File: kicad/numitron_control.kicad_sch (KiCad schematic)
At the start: 12 parts, among them U1 TLC5916IN, U2 IV-12, U3 TLC5916IN, U4 IV-12, U5 TLC5916IN, U6 IV-12, U7 TLC5916IN, U8 IV-12

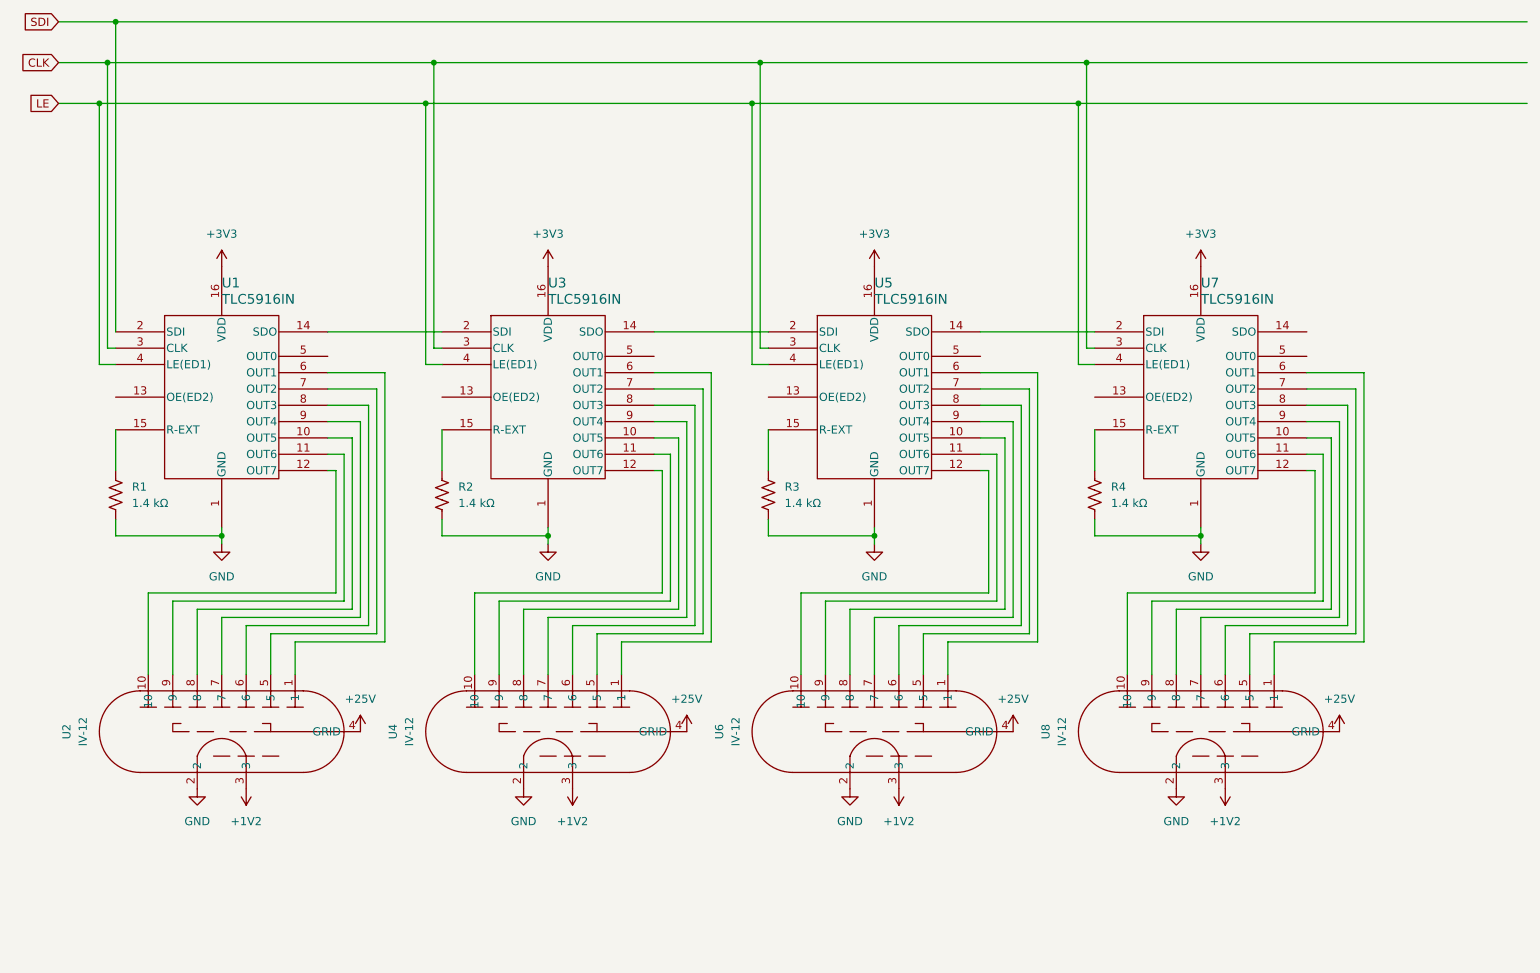
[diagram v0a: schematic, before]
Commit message: added voltage regulators, changed bit register
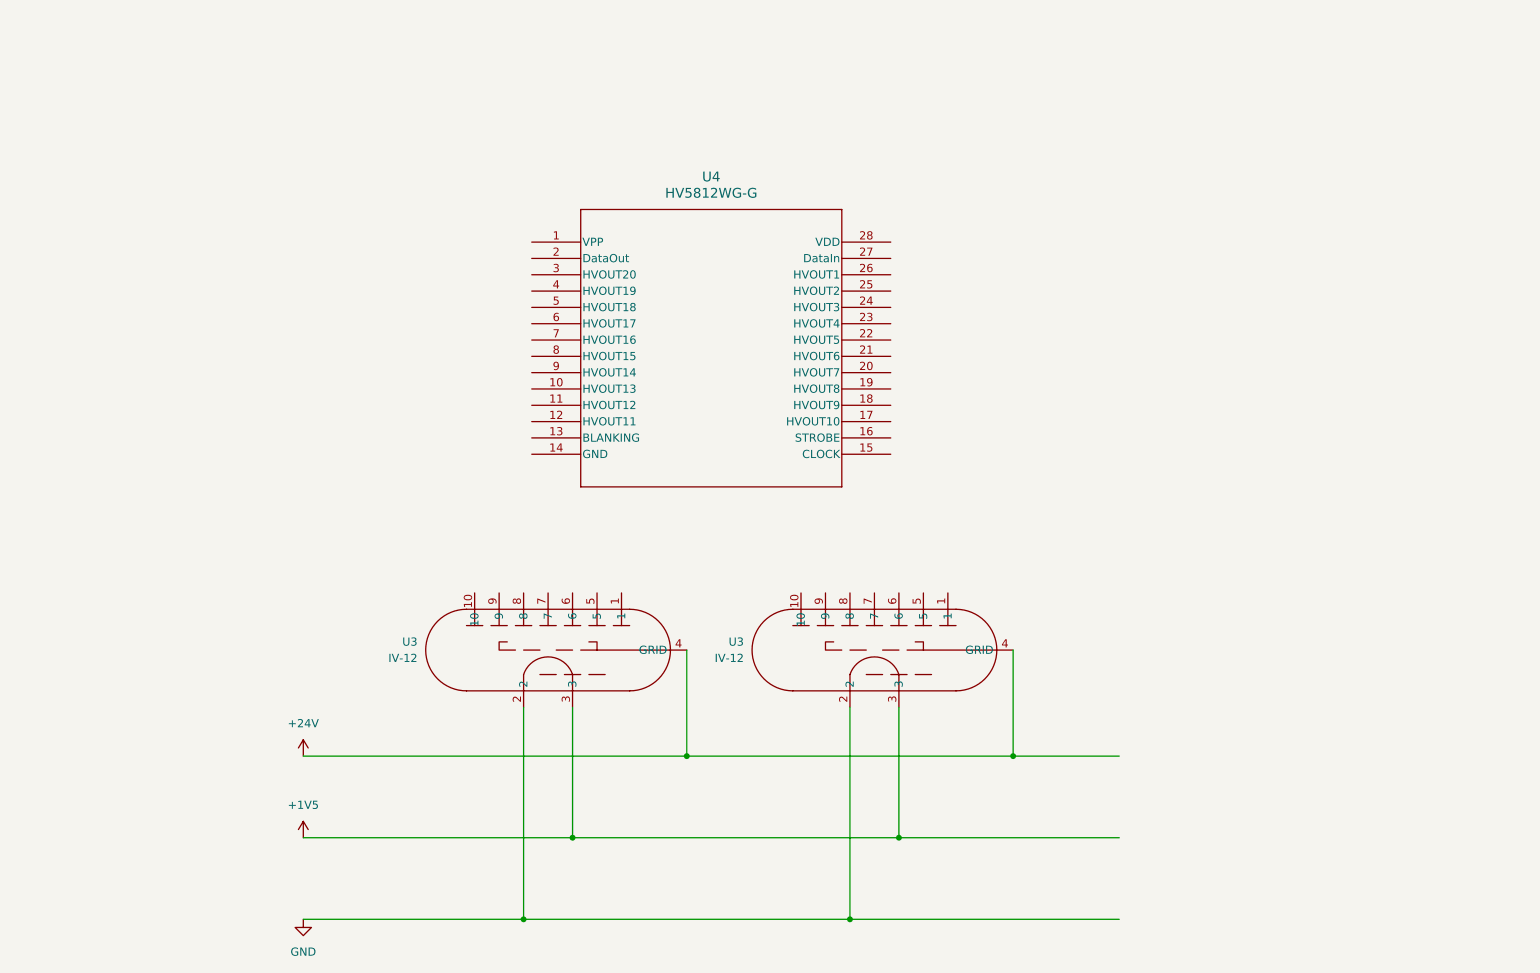
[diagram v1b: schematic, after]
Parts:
- removed R1, R2, R3, R4: 1.4 kΩ, symbol Device:R_US
- removed U1, U3, U5, U7: TLC5916IN, N16, symbol New_Library:TLC5916IN
- removed U4, U6, U8: IV-12, symbol New_Library:IV-12
- added U3: IV-12, symbol New_Library:IV-12
- added U4: HV5812WG-G, SOW28_17P90X7P50_MCH, symbol New_Library:HV5812WG-G
- renumbered U2 to U3
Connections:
- net GND: now also U3.2
- net +1V2 renamed +1V5
- net +1V5: now also U3.3
- net +25V renamed +24V
- net +24V: now also U3.4 (GRID)
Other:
- moved on the sheet: U3
